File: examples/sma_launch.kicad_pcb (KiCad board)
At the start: 4 copper layers, 30 x 14 mm, 3 parts, among them J7 732511151

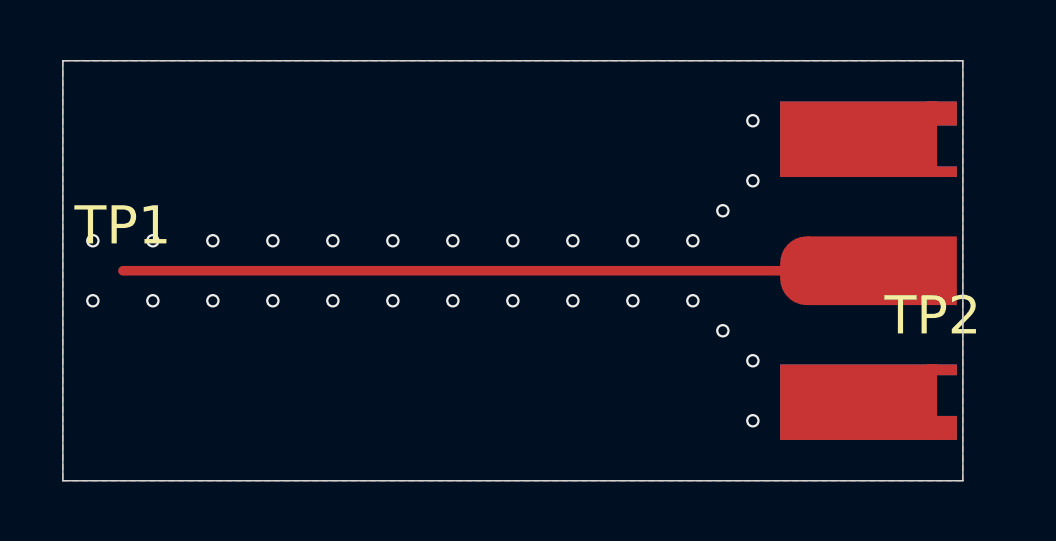
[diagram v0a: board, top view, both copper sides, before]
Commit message: examples: sma_launch is the straight launch, without the taper
The straight 0.32 mm line onto the connector pad matched better than the drawn taper (openEMS: worst S11
-22 dB against -13 to -15 dB), so it becomes the example and the variants go. Reference results, the
golden board summary and the line-model test follow the new board.

Co-Authored-By: Claude Opus 5.5 <noreply@anthropic.com>
Claude-Session: https://claude.ai/code/session_014teUjWwnXfXYChuStaHR5J
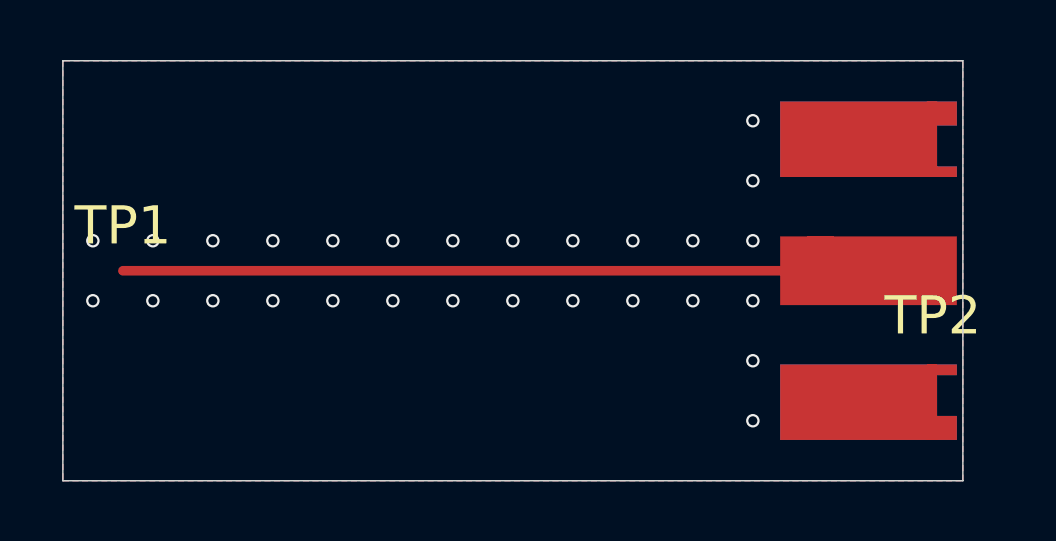
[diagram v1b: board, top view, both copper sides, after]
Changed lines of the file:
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@@
 			(solder_paste_margin -0.05)
 		)
-		(pad "inner" smd oval
+		(pad "inner" smd rect
 			(at 5 0 180)
 			(size 1.78 2.29)
@@
 				(best_length_ratio 1.5)
 				(max_length 2)
-				(best_width_ratio 1.5)
+				(best_width_ratio 1)
 				(max_width 2.5)
 				(curved_edges no)
 				(filter_ratio 0.9)
-				(enabled yes)
+				(enabled no)
 				(allow_two_segments yes)
 				(prefer_zone_connections yes)
@@
 	)
 	(via
-		(at 22 9)
+		(at 23 8)
 		(size 0.45)
 		(drill 0.3)
@@
 	)
 	(via
-		(at 22 5)
+		(at 23 6)
 		(size 0.45)
 		(drill 0.3)
@@
 	)
 	(zone
-		(net "/REF_SMA_N")
 		(layer "F.Cu")
-		(hatch none 0.1)
-		(priority 30002)
-		(attr
-			(teardrop
-				(type padvia)
-			)
-		)
-		(connect_pads yes
+		(hatch edge 0.5)
+		(connect_pads
 			(clearance 0)
 		)
-		(min_thickness 0.0254)
-		(fill yes
-			(island_removal_mode 1)
+		(min_thickness 0.25)
+		(keepout
+			(tracks allowed)
+			(vias allowed)
+			(pads allowed)
+			(copperpour not_allowed)
+			(footprints allowed)
+		)
+		(placement
+			(enabled no)
+			(sheetname "")
+		)
+		(fill
+			(thermal_gap 0.5)
+			(thermal_bridge_width 0.5)
+			(island_removal_mode 0)
 		)
 		(polygon
 			(pts
-				(xy 25.910001 7.16) (xy 25.910001 6.84) (xy 25.584911 6.325457) (xy 23.909001 7) (xy 25.584911 7.674543)
-			)
-		)
-	)
-	(zone
-		(net "/REF_SMA_N")
-		(layer "F.Cu")
-		(hatch none 0.1)
-		(priority 30000)
-		(attr
-			(teardrop
-				(type padvia)
-			)
-		)
-		(connect_pads yes
-			(clearance 0)
-		)
-		(min_thickness 0.0254)
-		(fill yes
-			(island_removal_mode 1)
-		)
-		(polygon
-			(pts
-				(xy 21.910001 6.84) (xy 21.910001 7.16) (xy 24.541648 8.106677) (xy 24.801001 7) (xy 24.541648 5.893323)
-			)
-		)
-	)
-	(zone
-		(net "/REF_SMA_N")
-		(layer "F.Cu")
-		(hatch none 0.1)
-		(priority 30001)
-		(attr
-			(teardrop
-				(type padvia)
-			)
-		)
-		(connect_pads yes
-			(clearance 0)
-		)
-		(min_thickness 0.0254)
-		(fill yes
-			(island_removal_mode 1)
-		)
-		(polygon
-			(pts
-				(xy 27.690001 7.16) (xy 27.690001 6.84) (xy 25.058354 5.893323) (xy 24.799001 7) (xy 25.058354 8.106677)
+				(xy 23.71 3.9) (xy 23.71 10.1) (xy 30 10.1) (xy 30 3.9)
 			)
 		)
@@
 	)
 	(zone
-		(layers "F.Cu" "In1.Cu" "In2.Cu")
+		(layers "In1.Cu" "In2.Cu")
 		(hatch edge 0.5)
 		(connect_pads
@@
 		(polygon
 			(pts
-				(xy 21.9 7) (xy 30 10.1) (xy 30 3.9)
-			)
-		)
+				(xy 23.9 3.9) (xy 23.9 10.1) (xy 30 10.1) (xy 30 3.9)
+			)
+		)
